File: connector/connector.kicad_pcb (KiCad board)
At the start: 2 copper layers, 18.7 x 4.8 mm, 15 parts, among them P11 CONN_1, P12 CONN_1, P13 CONN_1, P14 CONN_1, P15 CONN_1, P21 CONN_1, P22 CONN_1, P23 CONN_1, P24 CONN_1, P25 CONN_1

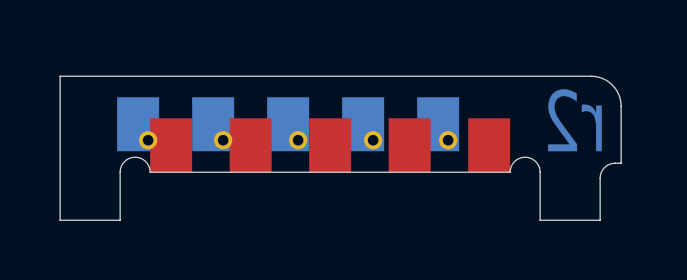
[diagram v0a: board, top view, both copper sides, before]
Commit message: Swap the front and pad pads of the first connection.
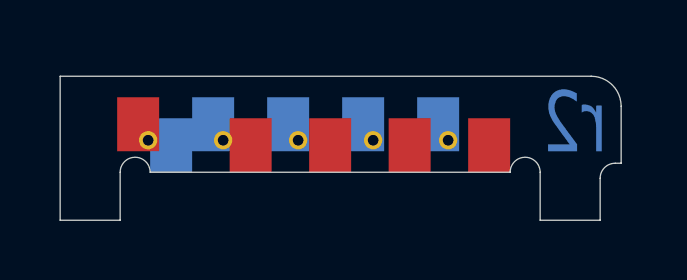
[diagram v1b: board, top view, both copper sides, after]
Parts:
- P11: footprint vertical_pcb_pad -> UGL:UHK_vertical_PCB_pad; moved to B.Cu
- P21: moved to F.Cu
- moved P11 1.63 mm to (142.1, 99.9)
- moved P21 0.59 mm to (141.0, 99.2)
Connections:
- P11 pad : N-000001 -> (no net)
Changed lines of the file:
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@@
 (kicad_pcb (version 4) (host pcbnew "(2014-jul-16 BZR unknown)-product")
   (general
-    (links 5)
-    (no_connects 5)
-    (area 108.35 78.7 182.578568 104.3542)
+    (links 4)
+    (no_connects 4)
+    (area 108.35 78.7 182.578568 104.38168)
     (thickness 1.6002)
     (drawings 22)
@@
     (pad_to_mask_clearance 0.1016)
     (aux_axis_origin 0 0)
-    (visible_elements FFFFFF7F)
+    (visible_elements FFFFEF7F)
     (pcbplotparams
       (layerselection 0x000f0_80000001)
@@
     (add_net N-000005)
   )
-  (module UGL:UHK_vertical_PCB_pad (layer Back)
-    (at 141.59 99.2)
-    (fp_text reference P21 (at 0 3.3) (layer B.SilkS) hide
-      (effects (font (thickness 0.3048)) (justify mirror))
-    )
-    (fp_text value CONN_1 (at 0 -2.9) (layer B.SilkS) hide
-      (effects (font (thickness 0.3048)) (justify mirror))
-    )
-    (pad "" smd rect (at -0.59 0) (size 1.4 1.8) (layers Back B.Mask)
-      (net 1 N-000001))
-  )
-  (module vertical_pcb_pad (layer Front)
-    (at 141 98.7)
-    (fp_text reference P11 (at 0 -3.3) (layer F.SilkS) hide
-      (effects (font (thickness 0.3048)))
-    )
-    (fp_text value CONN_1 (at 0 2.9) (layer F.SilkS) hide
-      (effects (font (thickness 0.3048)))
-    )
-    (pad "" smd rect (at 1.1 1.2) (size 1.4 1.8) (layers Front F.Mask)
-      (net 1 N-000001))
-  )
   (module vertical_pcb_pad (layer Back)
     (at 151.75 99.2)
@@
       (solder_mask_margin -1))
   )
+  (module UGL:UHK_vertical_PCB_pad (layer Back)
+    (at 142.1 99.9)
+    (fp_text reference P11 (at 0 3.3) (layer B.SilkS) hide
+      (effects (font (thickness 0.3048)) (justify mirror))
+    )
+    (fp_text value CONN_1 (at 0 -2.9) (layer B.SilkS) hide
+      (effects (font (thickness 0.3048)) (justify mirror))
+    )
+    (pad "" smd rect (at 0 0) (size 1.4 1.8) (layers Back B.Mask))
+  )
+  (module UGL:UHK_vertical_PCB_pad (layer Front)
+    (at 141 99.2)
+    (fp_text reference P21 (at 0 -3.3) (layer F.SilkS) hide
+      (effects (font (thickness 0.3048)))
+    )
+    (fp_text value CONN_1 (at 0 2.9) (layer F.SilkS) hide
+      (effects (font (thickness 0.3048)))
+    )
+    (pad "" smd rect (at 0 0) (size 1.4 1.8) (layers Front F.Mask)
+      (net 1 N-000001))
+  )
   (gr_text "< pin contact line" (at 167.9 98.6) (layer Eco1.User)

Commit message: Swap the top and bottom pads of the second connection.
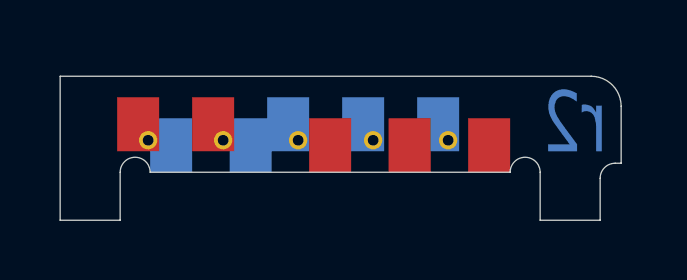
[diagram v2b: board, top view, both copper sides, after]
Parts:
- P12: footprint vertical_pcb_pad -> UGL:UHK_vertical_PCB_pad; moved to B.Cu
- P22: footprint vertical_pcb_pad -> UGL:UHK_vertical_PCB_pad; moved to F.Cu
- moved P12 1.73 mm to (144.8, 99.9)
- moved P22 0.63 mm to (143.5, 99.2)
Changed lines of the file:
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@@
   (general
     (links 4)
-    (no_connects 4)
+    (no_connects 3)
     (area 108.35 78.7 182.578568 104.38168)
     (thickness 1.6002)
@@
     (add_net N-000005)
   )
+  (module UGL:UHK_vertical_PCB_pad (layer Back)
+    (at 144.75 99.9)
+    (fp_text reference P12 (at 0 3.3) (layer B.SilkS) hide
+      (effects (font (thickness 0.3048)) (justify mirror))
+    )
+    (fp_text value CONN_1 (at 0 -2.9) (layer B.SilkS) hide
+      (effects (font (thickness 0.3048)) (justify mirror))
+    )
+    (pad "" smd rect (at 0 0) (size 1.4 1.8) (layers Back B.Mask)
+      (net 2 N-000002))
+  )
+  (module UGL:UHK_vertical_PCB_pad (layer Front)
+    (at 143.5 99.2)
+    (fp_text reference P22 (at 0 -3.3) (layer F.SilkS) hide
+      (effects (font (thickness 0.3048)))
+    )
+    (fp_text value CONN_1 (at 0 2.9) (layer F.SilkS) hide
+      (effects (font (thickness 0.3048)))
+    )
+    (pad "" smd rect (at 0 0) (size 1.4 1.8) (layers Front F.Mask)
+      (net 2 N-000002))
+  )
   (module vertical_pcb_pad (layer Back)
     (at 151.75 99.2)
@@
       (net 3 N-000003))
   )
-  (module vertical_pcb_pad (layer Back)
-    (at 144.13 99.2)
-    (fp_text reference P22 (at 0 3.3) (layer B.SilkS) hide
-      (effects (font (thickness 0.3048)) (justify mirror))
-    )
-    (fp_text value CONN_1 (at 0 -2.9) (layer B.SilkS) hide
-      (effects (font (thickness 0.3048)) (justify mirror))
-    )
-    (pad "" smd rect (at -0.63 0) (size 1.4 1.8) (layers Back B.Mask)
-      (net 2 N-000002))
-  )
   (module vertical_pcb_pad (layer Front)
     (at 148.5 98.7)
@@
       (net 3 N-000003))
   )
-  (module vertical_pcb_pad (layer Front)
-    (at 143.5 98.7)
-    (fp_text reference P12 (at 0 -3.3) (layer F.SilkS) hide
-      (effects (font (thickness 0.3048)))
-    )
-    (fp_text value CONN_1 (at 0 2.9) (layer F.SilkS) hide
-      (effects (font (thickness 0.3048)))
-    )
-    (pad "" smd rect (at 1.25 1.2) (size 1.4 1.8) (layers Front F.Mask)
-      (net 2 N-000002))
-  )
   (module UGL:via_24_14mil (layer Front)

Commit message: Swap the top and bottom pads of the third connection.
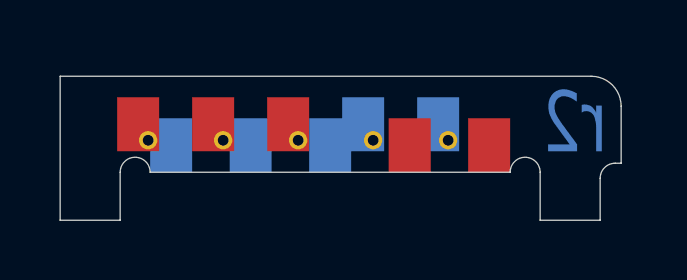
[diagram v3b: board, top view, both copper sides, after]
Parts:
- P13: footprint vertical_pcb_pad -> UGL:UHK_vertical_PCB_pad; moved to B.Cu
- P23: footprint vertical_pcb_pad -> UGL:UHK_vertical_PCB_pad; moved to F.Cu
- moved P13 1.84 mm to (147.4, 99.9)
- moved P23 0.67 mm to (146.0, 99.2)
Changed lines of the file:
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@@
       (net 4 N-000004))
-  )
-  (module vertical_pcb_pad (layer Back)
-    (at 146.67 99.2)
-    (fp_text reference P23 (at 0 3.3) (layer B.SilkS) hide
-      (effects (font (thickness 0.3048)) (justify mirror))
-    )
-    (fp_text value CONN_1 (at 0 -2.9) (layer B.SilkS) hide
-      (effects (font (thickness 0.3048)) (justify mirror))
-    )
-    (pad "" smd rect (at -0.67 0) (size 1.4 1.8) (layers Back B.Mask)
-      (net 3 N-000003))
   )
   (module vertical_pcb_pad (layer Front)
@@
     (pad "" smd rect (at 1.55 1.2) (size 1.4 1.8) (layers Front F.Mask)
       (net 4 N-000004))
-  )
-  (module vertical_pcb_pad (layer Front)
-    (at 146 98.7)
-    (fp_text reference P13 (at 0 -3.3) (layer F.SilkS) hide
-      (effects (font (thickness 0.3048)))
-    )
-    (fp_text value CONN_1 (at 0 2.9) (layer F.SilkS) hide
-      (effects (font (thickness 0.3048)))
-    )
-    (pad "" smd rect (at 1.4 1.2) (size 1.4 1.8) (layers Front F.Mask)
-      (net 3 N-000003))
   )
   (module UGL:via_24_14mil (layer Front)
@@
       (net 1 N-000001))
   )
+  (module UGL:UHK_vertical_PCB_pad (layer Front)
+    (at 146 99.2)
+    (fp_text reference P23 (at 0 -3.3) (layer F.SilkS) hide
+      (effects (font (thickness 0.3048)))
+    )
+    (fp_text value CONN_1 (at 0 2.9) (layer F.SilkS) hide
+      (effects (font (thickness 0.3048)))
+    )
+    (pad "" smd rect (at 0 0) (size 1.4 1.8) (layers Front F.Mask)
+      (net 3 N-000003))
+  )
+  (module UGL:UHK_vertical_PCB_pad (layer Back)
+    (at 147.4 99.9)
+    (fp_text reference P13 (at 0 3.3) (layer B.SilkS) hide
+      (effects (font (thickness 0.3048)) (justify mirror))
+    )
+    (fp_text value CONN_1 (at 0 -2.9) (layer B.SilkS) hide
+      (effects (font (thickness 0.3048)) (justify mirror))
+    )
+    (pad "" smd rect (at 0 0) (size 1.4 1.8) (layers Back B.Mask)
+      (net 3 N-000003))
+  )
   (gr_text "< pin contact line" (at 167.9 98.6) (layer Eco1.User)

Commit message: Swap the top and bottom pads of the fourth connection.
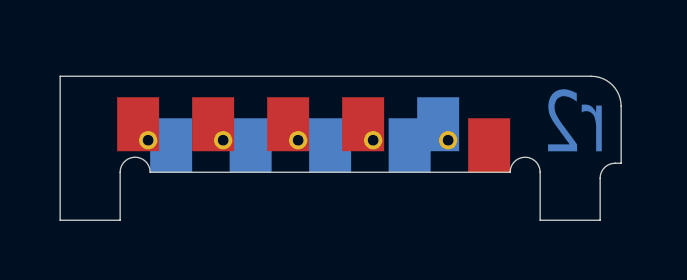
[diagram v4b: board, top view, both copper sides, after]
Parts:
- P14: footprint vertical_pcb_pad -> UGL:UHK_vertical_PCB_pad; moved to B.Cu
- P24: footprint vertical_pcb_pad -> UGL:UHK_vertical_PCB_pad; moved to F.Cu
- moved P14 1.96 mm to (150.1, 99.9)
- moved P24 0.71 mm to (148.5, 99.2)
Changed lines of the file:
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@@
   (general
     (links 4)
-    (no_connects 3)
+    (no_connects 4)
     (area 108.35 78.7 182.578568 104.38168)
     (thickness 1.6002)
@@
       (net 5 N-000005))
   )
-  (module vertical_pcb_pad (layer Back)
-    (at 149.21 99.2)
-    (fp_text reference P24 (at 0 3.3) (layer B.SilkS) hide
-      (effects (font (thickness 0.3048)) (justify mirror))
-    )
-    (fp_text value CONN_1 (at 0 -2.9) (layer B.SilkS) hide
-      (effects (font (thickness 0.3048)) (justify mirror))
-    )
-    (pad "" smd rect (at -0.71 0) (size 1.4 1.8) (layers Back B.Mask)
-      (net 4 N-000004))
-  )
-  (module vertical_pcb_pad (layer Front)
-    (at 148.5 98.7)
-    (fp_text reference P14 (at 0 -3.3) (layer F.SilkS) hide
-      (effects (font (thickness 0.3048)))
-    )
-    (fp_text value CONN_1 (at 0 2.9) (layer F.SilkS) hide
-      (effects (font (thickness 0.3048)))
-    )
-    (pad "" smd rect (at 1.55 1.2) (size 1.4 1.8) (layers Front F.Mask)
-      (net 4 N-000004))
-  )
   (module UGL:via_24_14mil (layer Front)
     (at 151.333334 99.733333)
@@
       (net 3 N-000003))
   )
+  (module UGL:UHK_vertical_PCB_pad (layer Front)
+    (at 148.5 99.2)
+    (fp_text reference P24 (at 0 -3.3) (layer F.SilkS) hide
+      (effects (font (thickness 0.3048)))
+    )
+    (fp_text value CONN_1 (at 0 2.9) (layer F.SilkS) hide
+      (effects (font (thickness 0.3048)))
+    )
+    (pad "" smd rect (at 0 0) (size 1.4 1.8) (layers Front F.Mask)
+      (net 4 N-000004))
+  )
+  (module UGL:UHK_vertical_PCB_pad (layer Back)
+    (at 150.05 99.9)
+    (fp_text reference P14 (at 0 3.3) (layer B.SilkS) hide
+      (effects (font (thickness 0.3048)) (justify mirror))
+    )
+    (fp_text value CONN_1 (at 0 -2.9) (layer B.SilkS) hide
+      (effects (font (thickness 0.3048)) (justify mirror))
+    )
+    (pad "" smd rect (at 0 0) (size 1.4 1.8) (layers Back B.Mask)
+      (net 4 N-000004))
+  )
   (gr_text "< pin contact line" (at 167.9 98.6) (layer Eco1.User)

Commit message: Swap the top and bottom pads of the fifth connection.
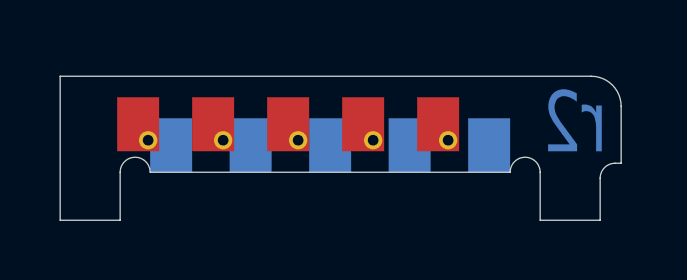
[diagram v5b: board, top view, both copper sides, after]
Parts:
- P15: footprint vertical_pcb_pad -> UGL:UHK_vertical_PCB_pad; moved to B.Cu
- P25: footprint vertical_pcb_pad -> UGL:UHK_vertical_PCB_pad; moved to F.Cu
- moved P15 2.08 mm to (152.7, 99.9)
- moved P25 0.75 mm to (151.0, 99.2)
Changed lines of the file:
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@@
   (general
     (links 4)
-    (no_connects 4)
+    (no_connects 3)
     (area 108.35 78.7 182.578568 104.38168)
     (thickness 1.6002)
@@
       (net 2 N-000002))
   )
-  (module vertical_pcb_pad (layer Back)
-    (at 151.75 99.2)
-    (fp_text reference P25 (at 0 3.3) (layer B.SilkS) hide
-      (effects (font (thickness 0.3048)) (justify mirror))
-    )
-    (fp_text value CONN_1 (at 0 -2.9) (layer B.SilkS) hide
-      (effects (font (thickness 0.3048)) (justify mirror))
-    )
-    (pad "" smd rect (at -0.75 0) (size 1.4 1.8) (layers Back B.Mask)
-      (net 5 N-000005))
-  )
-  (module vertical_pcb_pad (layer Front)
-    (at 151 98.7)
-    (fp_text reference P15 (at 0 -3.3) (layer F.SilkS) hide
-      (effects (font (thickness 0.3048)))
-    )
-    (fp_text value CONN_1 (at 0 2.9) (layer F.SilkS) hide
-      (effects (font (thickness 0.3048)))
-    )
-    (pad "" smd rect (at 1.7 1.2) (size 1.4 1.8) (layers Front F.Mask)
-      (net 5 N-000005))
-  )
   (module UGL:via_24_14mil (layer Front)
     (at 151.333334 99.733333)
@@
       (net 4 N-000004))
   )
+  (module UGL:UHK_vertical_PCB_pad (layer Front)
+    (at 151 99.2)
+    (fp_text reference P25 (at 0 -3.3) (layer F.SilkS) hide
+      (effects (font (thickness 0.3048)))
+    )
+    (fp_text value CONN_1 (at 0 2.9) (layer F.SilkS) hide
+      (effects (font (thickness 0.3048)))
+    )
+    (pad "" smd rect (at 0 0) (size 1.4 1.8) (layers Front F.Mask)
+      (net 5 N-000005))
+  )
+  (module UGL:UHK_vertical_PCB_pad (layer Back)
+    (at 152.7 99.9)
+    (fp_text reference P15 (at 0 3.3) (layer B.SilkS) hide
+      (effects (font (thickness 0.3048)) (justify mirror))
+    )
+    (fp_text value CONN_1 (at 0 -2.9) (layer B.SilkS) hide
+      (effects (font (thickness 0.3048)) (justify mirror))
+    )
+    (pad "" smd rect (at 0 0) (size 1.4 1.8) (layers Back B.Mask)
+      (net 5 N-000005))
+  )
   (gr_text "< pin contact line" (at 167.9 98.6) (layer Eco1.User)

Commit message: Reposition vias.
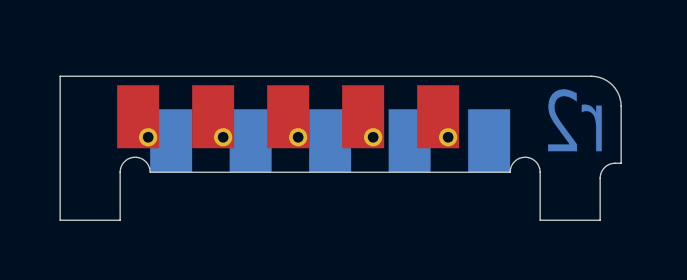
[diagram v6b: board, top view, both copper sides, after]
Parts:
- moved P21 0.25 mm to (141.0, 99.0)
- moved P22 0.25 mm to (143.5, 99.0)
- moved P23 0.25 mm to (146.0, 99.0)
- moved P24 0.25 mm to (148.5, 99.0)
- moved P25 0.25 mm to (151.0, 99.0)
- moved P11 0.15 mm to (142.1, 99.8)
- moved P12 0.15 mm to (144.8, 99.8)
- moved P13 0.15 mm to (147.4, 99.8)
- moved P14 0.15 mm to (150.1, 99.8)
- moved P15 0.15 mm to (152.7, 99.8)
- moved via_24_14mil 0.10 mm to (151.3, 99.6)
- moved via_24_14mil 0.10 mm to (148.8, 99.6)
- moved via_24_14mil 0.10 mm to (146.3, 99.6)
- moved via_24_14mil 0.10 mm to (143.8, 99.6)
- moved via_24_14mil 0.10 mm to (141.3, 99.6)
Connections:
- P11 pad : (no net) -> N-000001
